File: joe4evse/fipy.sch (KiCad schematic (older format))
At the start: 13 parts, among them J8 Conn_01x02, U3 FiPy, U4 MCP23S08-SO

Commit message: WIP: joe: Add errout signal
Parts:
- added J?: Conn_01x03, symbol Connector_Generic:Conn_01x03
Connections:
- net AC_TEST1: now also J?.1 (Pin_1); no longer U4.15 (IO5)
- new net: J?.2 (Pin_2), U4.15 (IO5)
- new net ERROUT: J?.3 (Pin_3)
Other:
- note added: "AC power stuck error signal"
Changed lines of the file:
@@
 Wire Wire Line
 	9000 2750 9750 2750
-Wire Wire Line
-	9000 2850 9750 2850
 Text Label 9750 2750 2    50   ~ 0
 AC_TEST0
-Text Label 9750 2850 2    50   ~ 0
+Text Label 10600 2650 2    50   ~ 0
 AC_TEST1
 Wire Wire Line
@@
 Wire Wire Line
 	7350 5950 7350 6050
+$Comp
+L Connector_Generic:Conn_01x03 J?
+U 1 1 5E5BD67B
+P 10150 2850
+F 0 "J?" H 10230 2892 50  0000 L CNN
+F 1 "Conn_01x03" H 10230 2801 50  0000 L CNN
+F 2 "" H 10150 2850 50  0001 C CNN
+F 3 "~" H 10150 2850 50  0001 C CNN
+	1    10150 2850
+	1    0    0    -1
+$EndComp
+Wire Wire Line
+	9000 2850 9950 2850
+Wire Wire Line
+	9950 2750 9850 2750
+Wire Wire Line
+	9850 2750 9850 2650
+Wire Wire Line
+	9950 2950 9850 2950
+Wire Wire Line
+	9850 2950 9850 3050
+Wire Wire Line
+	9850 2650 10600 2650
+Wire Wire Line
+	9850 3050 10600 3050
+Text Label 10600 3050 2    50   ~ 0
+ERROUT
+Wire Wire Line
+	2000 7150 2750 7150
+Text Label 2750 7150 2    50   ~ 0
+ERROUT
+Text HLabel 2000 7150 0    50   Output ~ 0
+ERROUT
+Text Notes 2850 7150 0    50   ~ 0
+AC power stuck error signal
 $EndSCHEMATC

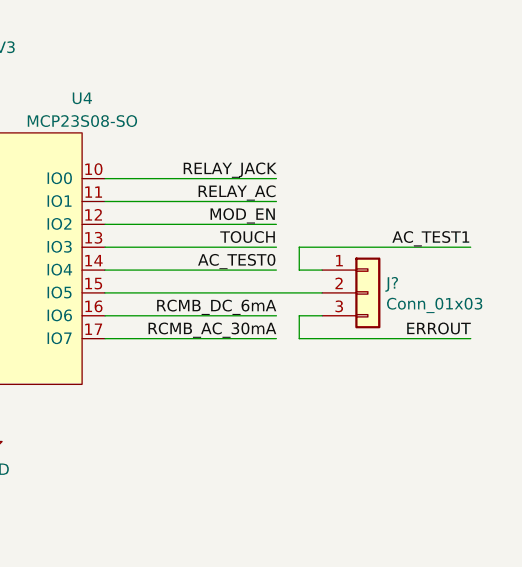
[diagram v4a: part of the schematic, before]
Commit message: joe/*: Add 0.1" header for easy access to RJ45 signals
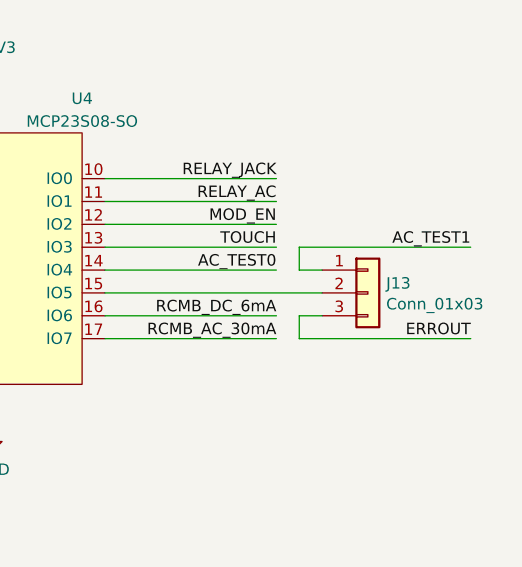
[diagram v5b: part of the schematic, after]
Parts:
- J13: renamed from J?; footprint (none) -> Connector_PinHeader_2.54mm:PinHeader_1x03_P2.54mm_Vertical
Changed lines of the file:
@@
 	7350 5950 7350 6050
 $Comp
-L Connector_Generic:Conn_01x03 J?
+L Connector_Generic:Conn_01x03 J13
 U 1 1 5E5BD67B
 P 10150 2850
-F 0 "J?" H 10230 2892 50  0000 L CNN
+F 0 "J13" H 10230 2892 50  0000 L CNN
 F 1 "Conn_01x03" H 10230 2801 50  0000 L CNN
-F 2 "" H 10150 2850 50  0001 C CNN
+F 2 "Connector_PinHeader_2.54mm:PinHeader_1x03_P2.54mm_Vertical" H 10150 2850 50  0001 C CNN
 F 3 "~" H 10150 2850 50  0001 C CNN
 	1    10150 2850

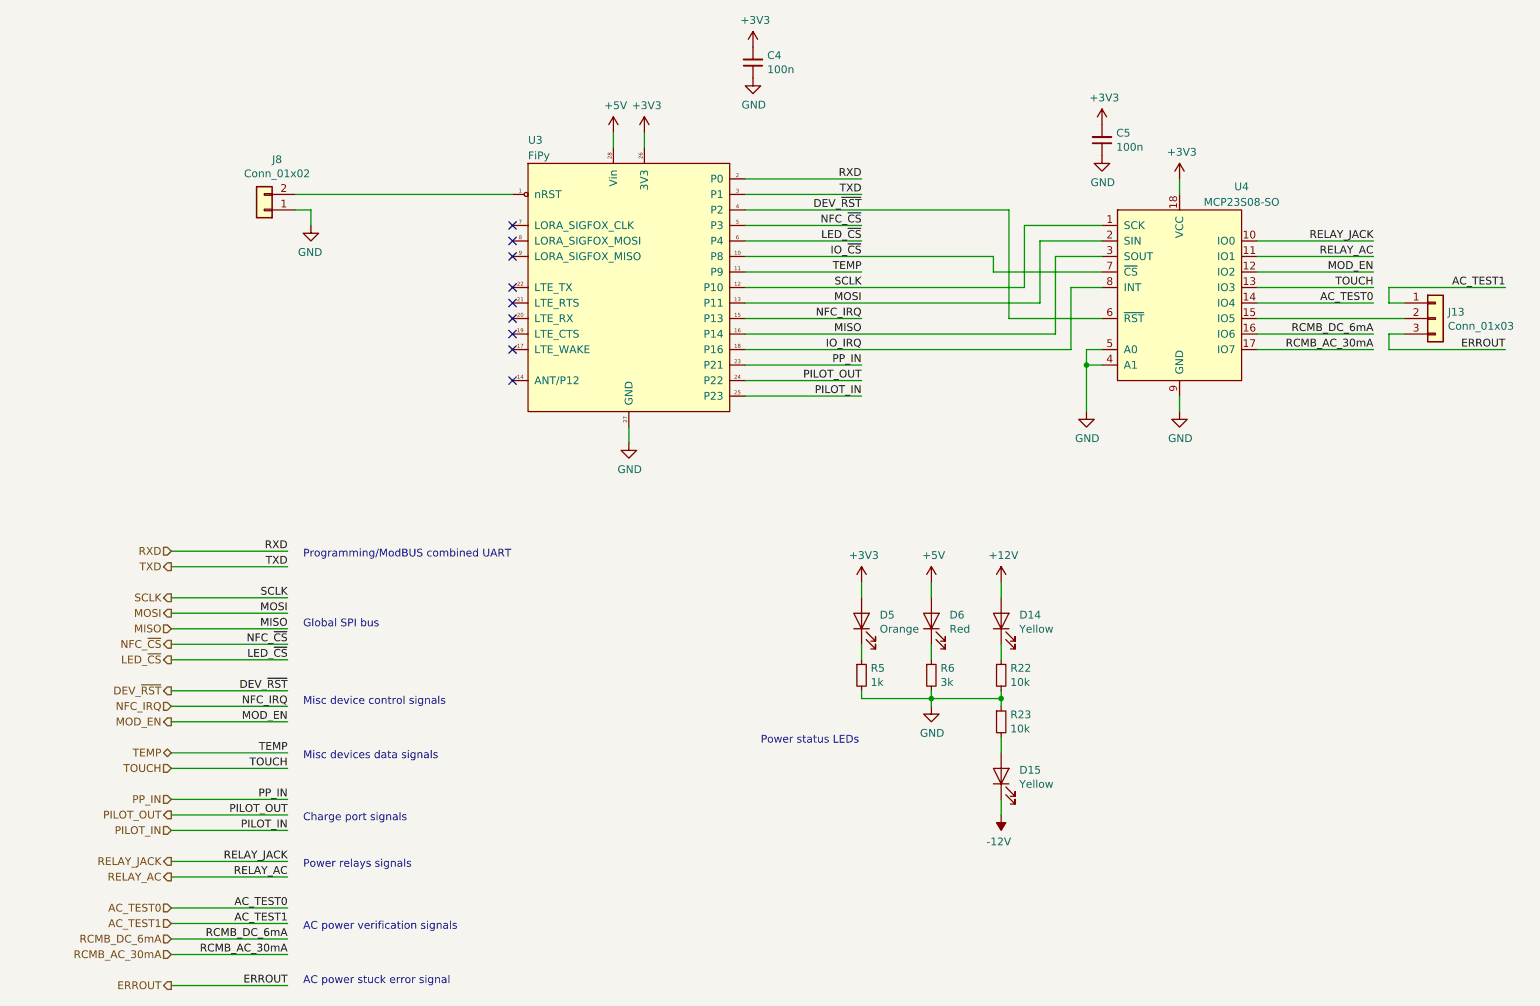
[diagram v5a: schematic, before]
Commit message: joe: Add 12V ERROUT
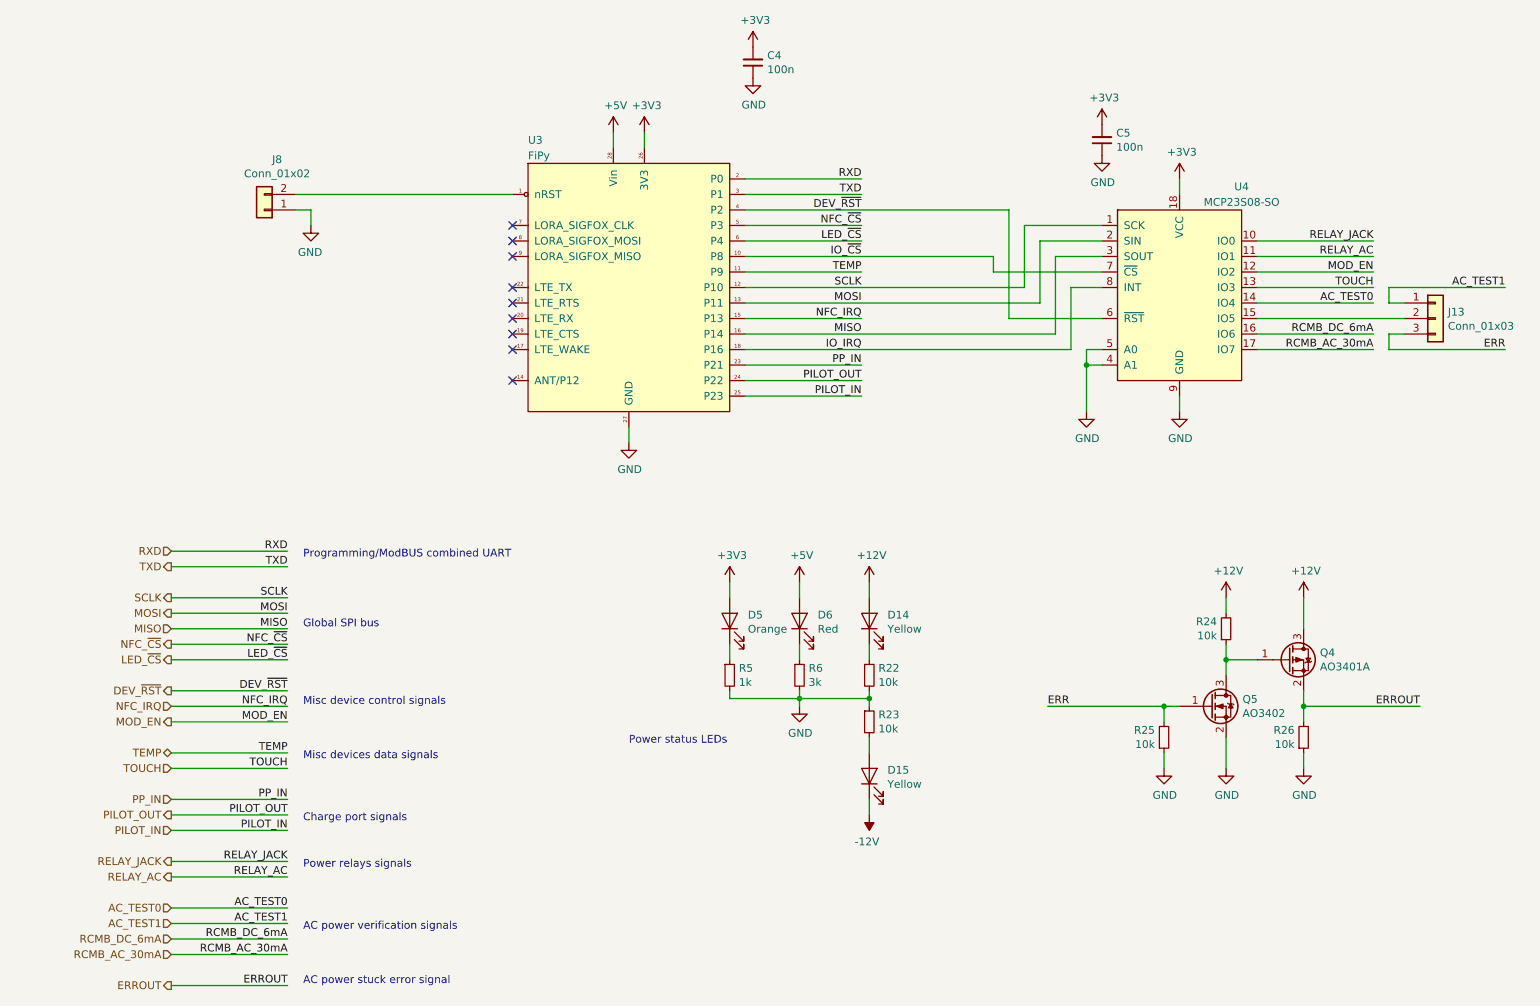
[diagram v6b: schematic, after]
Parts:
- added Q4: AO3401A, Package_TO_SOT_SMD:SOT-23, symbol Transistor_FET:AO3401A
- added Q5: AO3402, Package_TO_SOT_SMD:SOT-23, symbol ma4evse:AO3402
- added R24, R25, R26: 10k, Resistor_SMD:R_0603_1608Metric, symbol Device:R_Small
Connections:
- net +12V: now also Q4.3 (D), R24.2
- net ERROUT: now also Q4.2 (S), R26.2; no longer J13.3 (Pin_3)
- net GND: now also Q5.2 (S), R25.1, R26.1
- new net: Q4.1 (G), Q5.3 (D), R24.1
- new net ERR: J13.3 (Pin_3), Q5.1 (G), R25.2
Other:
- moved on the sheet: D14, D15, D5, D6, R22, R23, R5, R6

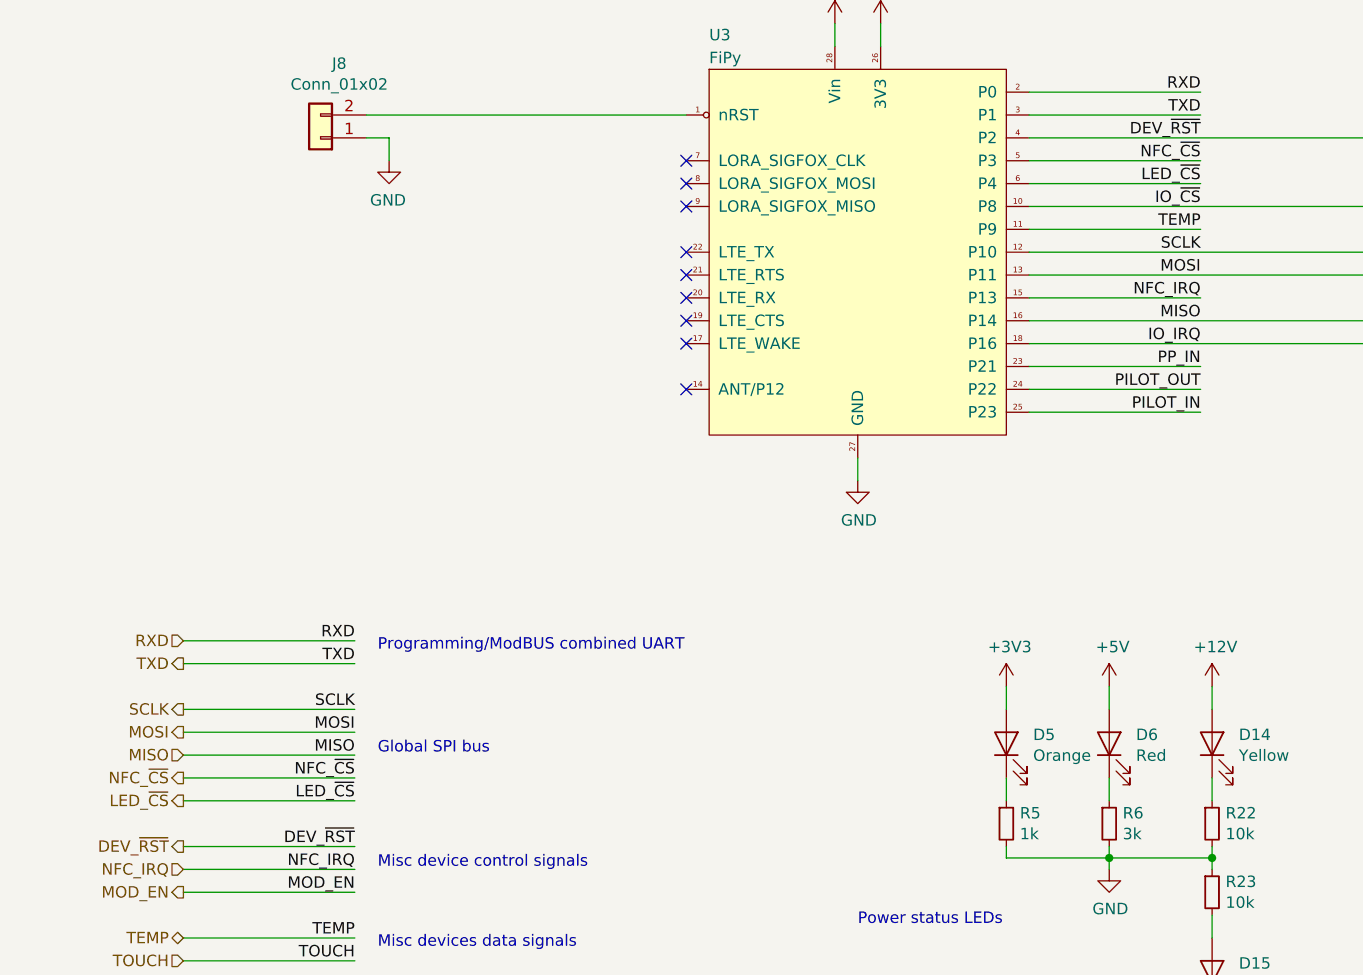
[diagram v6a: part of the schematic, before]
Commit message: joe/*: Rename LED_CS signal to LED_LAT
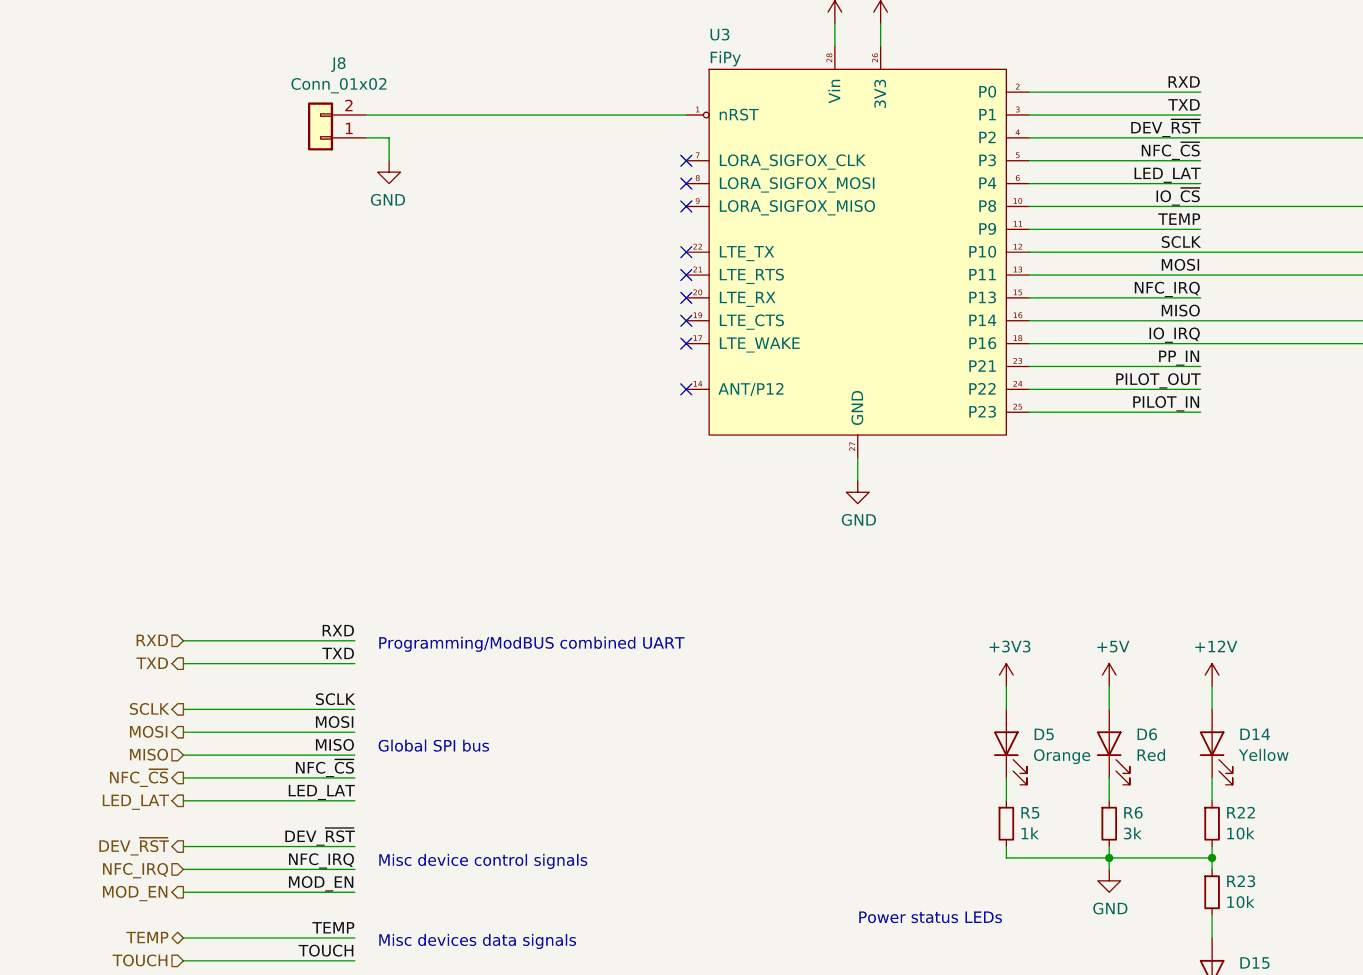
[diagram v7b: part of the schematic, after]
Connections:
- net LED_~CS renamed LED_LAT
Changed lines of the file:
@@
 NFC_~CS
 Text Label 6450 2350 2    50   ~ 0
-LED_~CS
+LED_LAT
 Text Label 6450 2650 2    50   ~ 0
 SCLK
@@
 NFC_~CS
 Text Label 2750 5050 2    50   ~ 0
-LED_~CS
+LED_LAT
 Text Label 2750 4650 2    50   ~ 0
 SCLK
@@
 NFC_~CS
 Text HLabel 2000 5050 0    50   Output ~ 0
-LED_~CS
+LED_LAT
 Text HLabel 2000 5250 0    50   Output ~ 0
 DEV_~RST

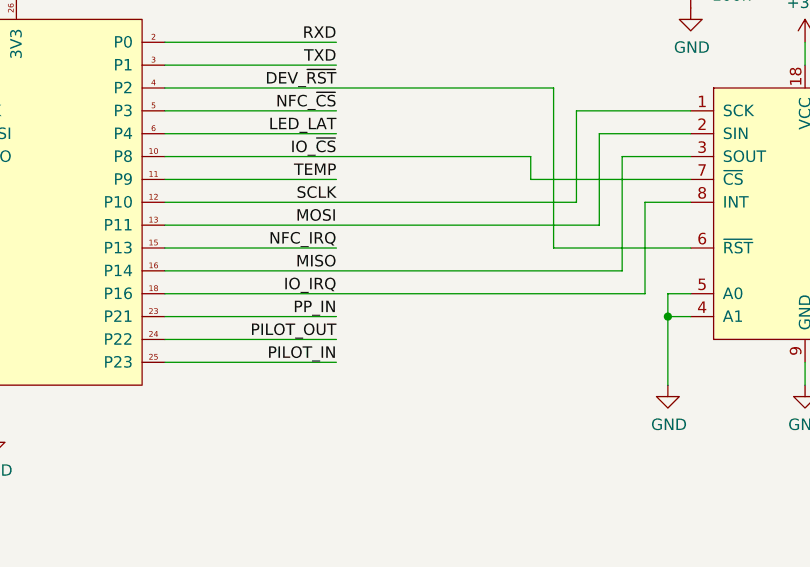
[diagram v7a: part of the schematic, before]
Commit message: joe/{sch, pcb}: Swap some MCU pins for easier pinout
- Swap P23/P13
- Swap P21/P16
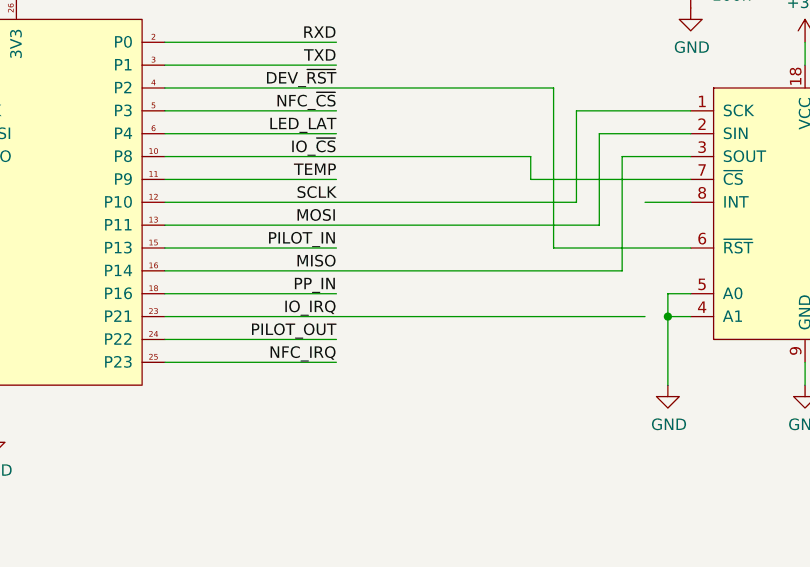
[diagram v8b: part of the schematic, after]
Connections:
- net IO_IRQ: now also U3.23 (P21); no longer U3.18 (P16), U4.8 (INT)
- net NFC_IRQ: now also U3.25 (P23); no longer U3.15 (P13)
- net PILOT_IN: now also U3.15 (P13); no longer U3.25 (P23)
- net PP_IN: now also U3.18 (P16); no longer U3.23 (P21)
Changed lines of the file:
@@
 NoConn ~ 4200 2750
 NoConn ~ 4200 2650
-Text Label 6450 2850 2    50   ~ 0
+Text Label 6450 3350 2    50   ~ 0
 NFC_IRQ
 Wire Wire Line
-	5700 2850 6450 2850
+	5700 3350 6450 3350
 Text Label 6450 2950 2    50   ~ 0
 MISO
@@
 Text Label 6450 3250 2    50   ~ 0
 PILOT_OUT
-Text Label 6450 3350 2    50   ~ 0
+Text Label 6450 2850 2    50   ~ 0
 PILOT_IN
 Wire Wire Line
 	5700 3250 6450 3250
 Wire Wire Line
-	6450 3350 5700 3350
+	6450 2850 5700 2850
 Wire Wire Line
-	5700 3150 6450 3150
-Text Label 6450 3150 2    50   ~ 0
+	5700 3050 6450 3050
+Text Label 6450 3050 2    50   ~ 0
 PP_IN
 Text Label 6450 2150 2    50   ~ 0
@@
 Text Label 6450 2450 2    50   ~ 0
 IO_~CS
-Text Label 6450 3050 2    50   ~ 0
+Text Label 6450 3150 2    50   ~ 0
 IO_IRQ
 $Comp
@@
 	5700 2650 7500 2650
 Wire Wire Line
-	7800 3050 7800 2650
-Wire Wire Line
 	7800 2650 8000 2650
 Wire Wire Line
-	5700 3050 7800 3050
+	5700 3150 7800 3150
 Wire Wire Line
 	7700 2950 7700 2450
